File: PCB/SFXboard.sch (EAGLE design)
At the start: 17 parts, among them J1 AVR_SPI_PRG_62X3_LOCK, J2 TERMBLOCK4POS, J3 POWER_JACKPTH, Q1 16MHz, Q2 BSS138, Q3 BSS138, Q4 BSS138, U1 ATMEGA16U2-AU, X1 USBSMD

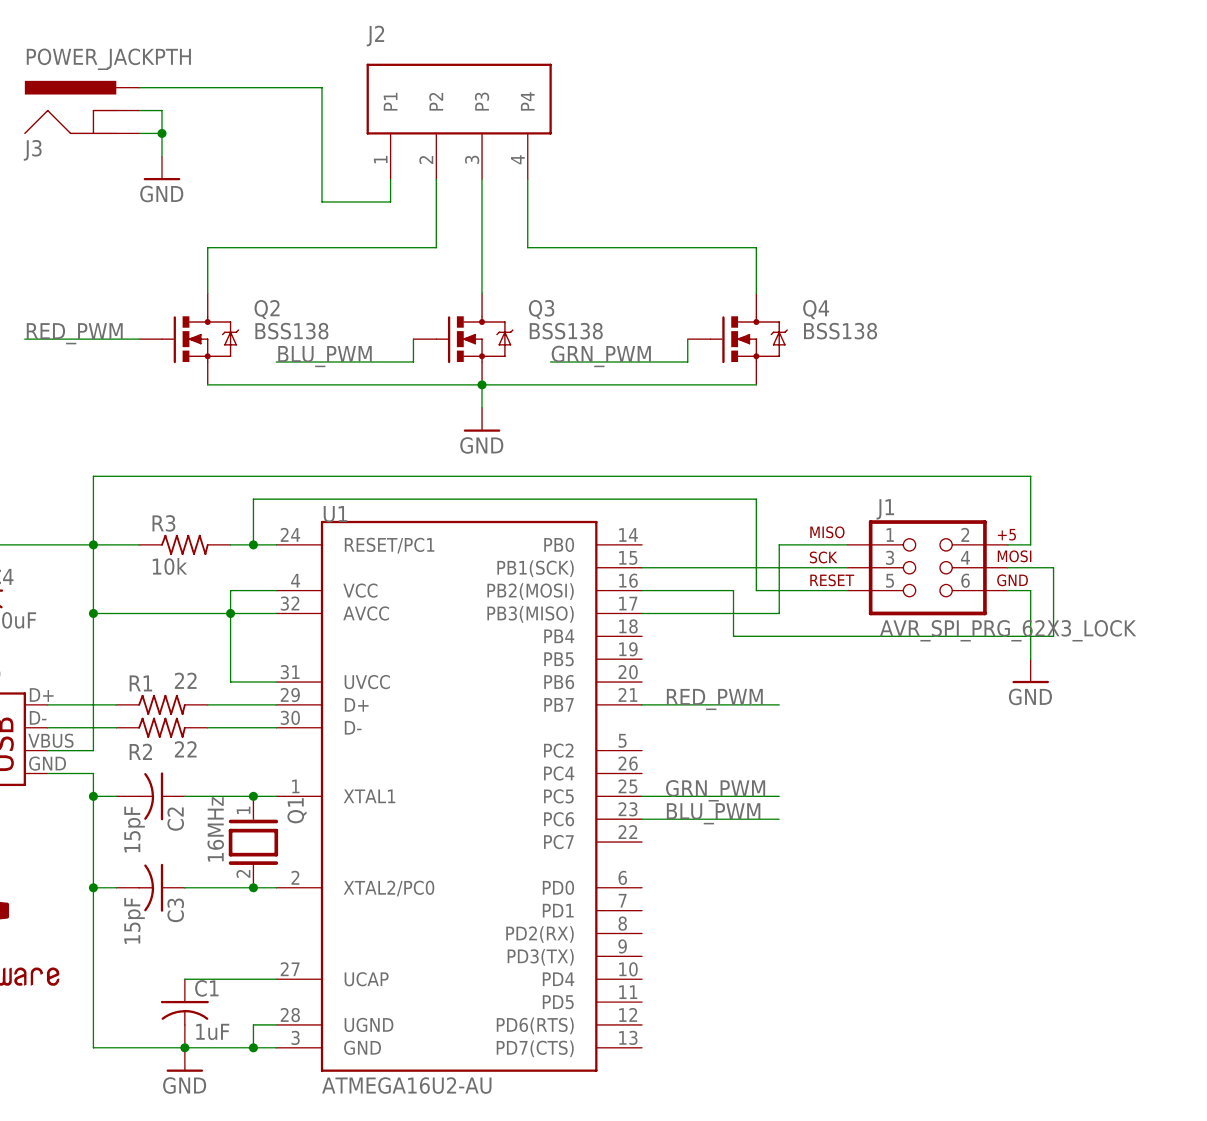
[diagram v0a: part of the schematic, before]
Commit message: Begin working on better power filtering, misc enhancements
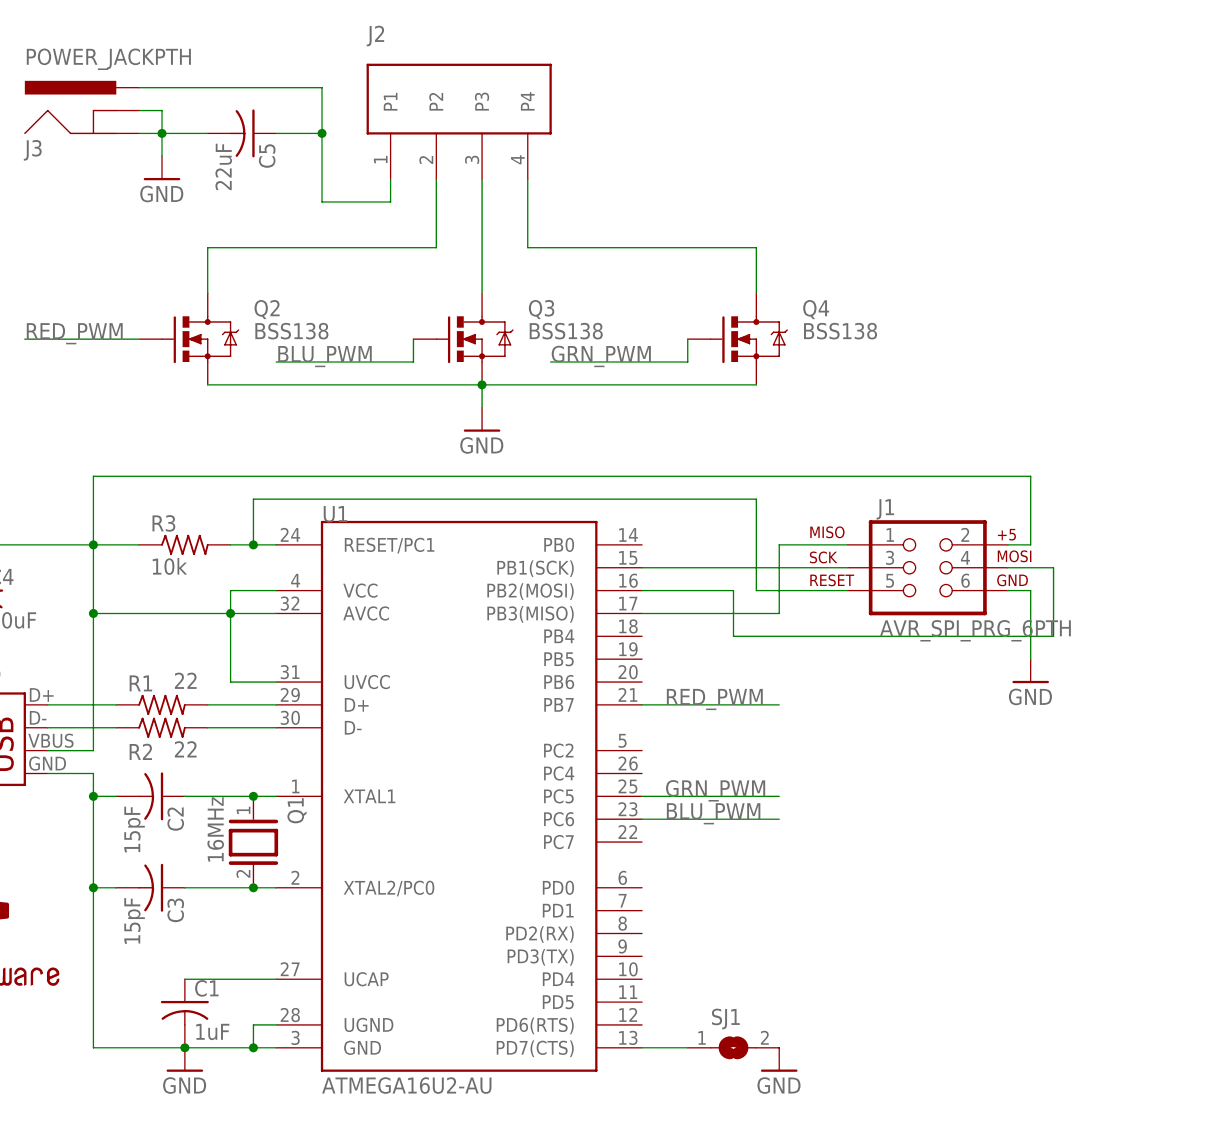
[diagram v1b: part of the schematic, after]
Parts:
- added C5: 22uF, resistor:C-USC0805
- added SJ1: (no value), jumper:SJ
- J1: value AVR_SPI_PRG_62X3_LOCK -> AVR_SPI_PRG_6PTH; device SparkFun-Connectors:AVR_SPI_PRG_62X3_LOCK -> SparkFun-Connectors:AVR_SPI_PRG_6PTH
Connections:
- new net N$17: SJ1.1, U1.PD7(CTS)
- net GND: now also C5.2, SJ1.2
- net N$16: now also C5.1
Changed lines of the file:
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@@
 <part name="C4" library="resistor" deviceset="C-US" device="C0805" value="10uF"/>
 <part name="GND3" library="supply1" deviceset="GND" device=""/>
-<part name="J1" library="SparkFun-Connectors" deviceset="AVR_SPI_PRG_6" device="2X3_LOCK"/>
+<part name="J1" library="SparkFun-Connectors" deviceset="AVR_SPI_PRG_6" device="PTH"/>
 <part name="GND4" library="supply1" deviceset="GND" device=""/>
 <part name="J2" library="sfxboard" deviceset="TERMBLOCK4POS" device=""/>
@@
 <part name="GND5" library="supply1" deviceset="GND" device=""/>
 <part name="U$2" library="SparkFun-Aesthetics" deviceset="OSHW-LOGO" device="S"/>
+<part name="C5" library="resistor" deviceset="C-US" device="C0805" value="22uF"/>
+<part name="SJ1" library="jumper" deviceset="SJ" device=""/>
+<part name="GND6" library="supply1" deviceset="GND" device=""/>
 </parts>
 <sheets>
@@
 <instance part="GND5" gate="1" x="-33.02" y="68.58"/>
 <instance part="U$2" gate="G$1" x="-55.88" y="-12.7"/>
+<instance part="C5" gate="G$1" x="-22.86" y="73.66" rot="R270"/>
+<instance part="SJ1" gate="1" x="30.48" y="-27.94"/>
+<instance part="GND6" gate="1" x="35.56" y="-30.48"/>
 </instances>
 <busses>
@@
 <pinref part="GND5" gate="1" pin="GND"/>
 <junction x="-33.02" y="73.66"/>
+<pinref part="C5" gate="G$1" pin="2"/>
+<wire x1="-27.94" y1="73.66" x2="-33.02" y2="73.66" width="0.1524" layer="91"/>
+</segment>
+<segment>
+<pinref part="SJ1" gate="1" pin="2"/>
+<pinref part="GND6" gate="1" pin="GND"/>
 </segment>
 </net>
@@
 <pinref part="J3" gate="G$1" pin="PWR"/>
 <wire x1="-35.56" y1="78.74" x2="-15.24" y2="78.74" width="0.1524" layer="91"/>
-<wire x1="-15.24" y1="78.74" x2="-15.24" y2="66.04" width="0.1524" layer="91"/>
+<wire x1="-15.24" y1="78.74" x2="-15.24" y2="73.66" width="0.1524" layer="91"/>
+<wire x1="-15.24" y1="73.66" x2="-15.24" y2="66.04" width="0.1524" layer="91"/>
 <wire x1="-15.24" y1="66.04" x2="-7.62" y2="66.04" width="0.1524" layer="91"/>
 <pinref part="J2" gate="G$1" pin="P1"/>
 <wire x1="-7.62" y1="66.04" x2="-7.62" y2="68.58" width="0.1524" layer="91"/>
+<pinref part="C5" gate="G$1" pin="1"/>
+<wire x1="-20.32" y1="73.66" x2="-15.24" y2="73.66" width="0.1524" layer="91"/>
+<junction x="-15.24" y="73.66"/>
 </segment>
 </net>
@@
 </segment>
 </net>
+<net name="N$17" class="0">
+<segment>
+<pinref part="SJ1" gate="1" pin="1"/>
+<pinref part="U1" gate="G$1" pin="PD7(CTS)"/>
+<wire x1="25.4" y1="-27.94" x2="20.32" y2="-27.94" width="0.1524" layer="91"/>
+</segment>
+</net>

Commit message: Circuit improvements, but not yet complete
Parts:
- added C6: 0.1uF, resistor:C-USC0402
- added F1: PTC0603, SparkFun-PowerIC:PTC0603
- added FRAME1: FRAME-LETTER, SparkFun-Aesthetics:FRAME-LETTER
- added R4, R5, R6: 470, resistor:R-US_R0805
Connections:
- new net B: R6.1, U1.PC6
- new net G: R5.1, U1.PC5
- new net N$18: C4.1, C6.1, F1.2, J1.2, R3.1, U1.AVCC, U1.UVCC, U1.VCC
- new net R: R4.1, U1.PB7
- net BLU_PWM: now also R6.2; no longer U1.PC6
- net GND: now also C6.2
- net GRN_PWM: now also R5.2; no longer U1.PC5
- net N$2: now also F1.1; no longer C4.1, J1.2, R3.1, U1.AVCC, U1.UVCC, U1.VCC
- net RED_PWM: now also R4.2; no longer U1.PB7
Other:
- note added: "Karl Koscher (supersat@cs.uw.edu)"
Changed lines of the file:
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@@
 <part name="SJ1" library="jumper" deviceset="SJ" device=""/>
 <part name="GND6" library="supply1" deviceset="GND" device=""/>
+<part name="C6" library="resistor" deviceset="C-US" device="C0402" value="0.1uF"/>
+<part name="GND7" library="supply1" deviceset="GND" device=""/>
+<part name="R4" library="resistor" deviceset="R-US_" device="R0805" value="470"/>
+<part name="R5" library="resistor" deviceset="R-US_" device="R0805" value="470"/>
+<part name="R6" library="resistor" deviceset="R-US_" device="R0805" value="470"/>
+<part name="FRAME1" library="SparkFun-Aesthetics" deviceset="FRAME-LETTER" device=""/>
+<part name="F1" library="SparkFun-PowerIC" deviceset="PTC" device="0603"/>
 </parts>
 <sheets>
 <sheet>
 <plain>
+<text x="26.67" y="-79.248" size="2.54" layer="94">Karl Koscher (supersat@cs.uw.edu)</text>
 </plain>
 <instances>
@@
 <instance part="C1" gate="G$1" x="-30.48" y="-22.86"/>
 <instance part="GND1" gate="1" x="-30.48" y="-30.48"/>
-<instance part="X1" gate="G$1" x="-48.26" y="2.54" rot="MR0"/>
+<instance part="X1" gate="G$1" x="-60.96" y="2.54" rot="MR0"/>
 <instance part="R1" gate="G$1" x="-33.02" y="10.16" smashed="yes">
 <attribute name="NAME" x="-36.83" y="11.6586" size="1.778" layer="95"/>
@@
 <instance part="SJ1" gate="1" x="30.48" y="-27.94"/>
 <instance part="GND6" gate="1" x="35.56" y="-30.48"/>
+<instance part="C6" gate="G$1" x="-63.5" y="22.86"/>
+<instance part="GND7" gate="1" x="-63.5" y="15.24"/>
+<instance part="R4" gate="G$1" x="30.48" y="10.16"/>
+<instance part="R5" gate="G$1" x="30.48" y="0" smashed="yes">
+<attribute name="NAME" x="26.67" y="1.4986" size="1.778" layer="95"/>
+<attribute name="VALUE" x="31.75" y="1.778" size="1.778" layer="96"/>
+</instance>
+<instance part="R6" gate="G$1" x="30.48" y="-2.54" smashed="yes">
+<attribute name="NAME" x="26.67" y="-6.1214" size="1.778" layer="95"/>
+<attribute name="VALUE" x="31.75" y="-5.842" size="1.778" layer="96"/>
+</instance>
+<instance part="FRAME1" gate="G$1" x="-121.92" y="-86.36"/>
+<instance part="FRAME1" gate="G$2" x="25.4" y="-86.36"/>
+<instance part="F1" gate="G$1" x="-50.8" y="5.08"/>
 </instances>
 <busses>
@@
 <wire x1="-40.64" y1="-10.16" x2="-40.64" y2="0" width="0.1524" layer="91"/>
 <wire x1="-40.64" y1="0" x2="-40.64" y2="2.54" width="0.1524" layer="91"/>
-<wire x1="-40.64" y1="2.54" x2="-45.72" y2="2.54" width="0.1524" layer="91"/>
+<wire x1="-40.64" y1="2.54" x2="-58.42" y2="2.54" width="0.1524" layer="91"/>
 <pinref part="C2" gate="G$1" pin="2"/>
 <wire x1="-38.1" y1="0" x2="-40.64" y2="0" width="0.1524" layer="91"/>
@@
 <pinref part="GND6" gate="1" pin="GND"/>
 </segment>
-</net>
-<net name="N$2" class="0">
-<segment>
-<pinref part="U1" gate="G$1" pin="VCC"/>
-<wire x1="-20.32" y1="22.86" x2="-25.4" y2="22.86" width="0.1524" layer="91"/>
-<wire x1="-25.4" y1="22.86" x2="-25.4" y2="20.32" width="0.1524" layer="91"/>
-<pinref part="U1" gate="G$1" pin="AVCC"/>
-<wire x1="-25.4" y1="20.32" x2="-20.32" y2="20.32" width="0.1524" layer="91"/>
-<pinref part="U1" gate="G$1" pin="UVCC"/>
-<wire x1="-20.32" y1="12.7" x2="-25.4" y2="12.7" width="0.1524" layer="91"/>
-<wire x1="-25.4" y1="20.32" x2="-25.4" y2="12.7" width="0.1524" layer="91"/>
-<pinref part="X1" gate="G$1" pin="VBUS"/>
-<wire x1="-45.72" y1="5.08" x2="-40.64" y2="5.08" width="0.1524" layer="91"/>
-<wire x1="-40.64" y1="5.08" x2="-40.64" y2="20.32" width="0.1524" layer="91"/>
-<wire x1="-40.64" y1="20.32" x2="-25.4" y2="20.32" width="0.1524" layer="91"/>
-<junction x="-25.4" y="20.32"/>
-<pinref part="R3" gate="G$1" pin="1"/>
-<wire x1="-35.56" y1="27.94" x2="-40.64" y2="27.94" width="0.1524" layer="91"/>
-<wire x1="-40.64" y1="27.94" x2="-40.64" y2="20.32" width="0.1524" layer="91"/>
-<junction x="-40.64" y="20.32"/>
-<pinref part="C4" gate="G$1" pin="1"/>
-<wire x1="-53.34" y1="25.4" x2="-53.34" y2="27.94" width="0.1524" layer="91"/>
-<wire x1="-53.34" y1="27.94" x2="-40.64" y2="27.94" width="0.1524" layer="91"/>
-<junction x="-40.64" y="27.94"/>
-<pinref part="J1" gate="G$1" pin="2"/>
-<wire x1="60.96" y1="27.94" x2="63.5" y2="27.94" width="0.1524" layer="91"/>
-<wire x1="63.5" y1="27.94" x2="63.5" y2="35.56" width="0.1524" layer="91"/>
-<wire x1="63.5" y1="35.56" x2="-40.64" y2="35.56" width="0.1524" layer="91"/>
-<wire x1="-40.64" y1="35.56" x2="-40.64" y2="27.94" width="0.1524" layer="91"/>
+<segment>
+<pinref part="C6" gate="G$1" pin="2"/>
+<pinref part="GND7" gate="1" pin="GND"/>
 </segment>
 </net>
@@
 <pinref part="X1" gate="G$1" pin="D+"/>
 <pinref part="R1" gate="G$1" pin="1"/>
-<wire x1="-45.72" y1="10.16" x2="-38.1" y2="10.16" width="0.1524" layer="91"/>
+<wire x1="-58.42" y1="10.16" x2="-38.1" y2="10.16" width="0.1524" layer="91"/>
 </segment>
 </net>
@@
 <pinref part="X1" gate="G$1" pin="D-"/>
 <pinref part="R2" gate="G$1" pin="1"/>
-<wire x1="-45.72" y1="7.62" x2="-38.1" y2="7.62" width="0.1524" layer="91"/>
+<wire x1="-58.42" y1="7.62" x2="-38.1" y2="7.62" width="0.1524" layer="91"/>
 </segment>
 </net>
@@
 <net name="RED_PWM" class="0">
 <segment>
-<pinref part="U1" gate="G$1" pin="PB7"/>
-<wire x1="20.32" y1="10.16" x2="35.56" y2="10.16" width="0.1524" layer="91"/>
-<label x="22.86" y="10.16" size="1.778" layer="95"/>
-</segment>
-<segment>
 <pinref part="Q2" gate="G$1" pin="G"/>
 <wire x1="-35.56" y1="50.8" x2="-48.26" y2="50.8" width="0.1524" layer="91"/>
 <label x="-48.26" y="50.8" size="1.778" layer="95"/>
+</segment>
+<segment>
+<pinref part="R4" gate="G$1" pin="2"/>
+<wire x1="35.56" y1="10.16" x2="50.8" y2="10.16" width="0.1524" layer="91"/>
+<label x="38.1" y="10.16" size="1.778" layer="95"/>
 </segment>
 </net>
@@
 </segment>
 <segment>
-<pinref part="U1" gate="G$1" pin="PC6"/>
-<wire x1="20.32" y1="-2.54" x2="35.56" y2="-2.54" width="0.1524" layer="91"/>
-<label x="22.86" y="-2.54" size="1.778" layer="95"/>
+<pinref part="R6" gate="G$1" pin="2"/>
+<wire x1="35.56" y1="-2.54" x2="50.8" y2="-2.54" width="0.1524" layer="91"/>
+<label x="38.1" y="-2.54" size="1.778" layer="95"/>
 </segment>
 </net>
@@
 </segment>
 <segment>
-<pinref part="U1" gate="G$1" pin="PC5"/>
-<wire x1="20.32" y1="0" x2="35.56" y2="0" width="0.1524" layer="91"/>
-<label x="22.86" y="0" size="1.778" layer="95"/>
+<pinref part="R5" gate="G$1" pin="2"/>
+<wire x1="35.56" y1="0" x2="50.8" y2="0" width="0.1524" layer="91"/>
+<label x="38.1" y="0" size="1.778" layer="95"/>
 </segment>
 </net>
@@
 </segment>
 </net>
+<net name="R" class="0">
+<segment>
+<pinref part="U1" gate="G$1" pin="PB7"/>
+<wire x1="20.32" y1="10.16" x2="25.4" y2="10.16" width="0.1524" layer="91"/>
+<pinref part="R4" gate="G$1" pin="1"/>
+</segment>
+</net>
+<net name="G" class="0">
+<segment>
+<pinref part="U1" gate="G$1" pin="PC5"/>
+<wire x1="20.32" y1="0" x2="25.4" y2="0" width="0.1524" layer="91"/>
+<pinref part="R5" gate="G$1" pin="1"/>
+</segment>
+</net>
+<net name="B" class="0">
+<segment>
+<pinref part="U1" gate="G$1" pin="PC6"/>
+<wire x1="20.32" y1="-2.54" x2="25.4" y2="-2.54" width="0.1524" layer="91"/>
+<pinref part="R6" gate="G$1" pin="1"/>
+</segment>
+</net>
+<net name="N$18" class="0">
+<segment>
+<pinref part="U1" gate="G$1" pin="VCC"/>
+<wire x1="-20.32" y1="22.86" x2="-25.4" y2="22.86" width="0.1524" layer="91"/>
+<wire x1="-25.4" y1="22.86" x2="-25.4" y2="20.32" width="0.1524" layer="91"/>
+<pinref part="U1" gate="G$1" pin="AVCC"/>
+<wire x1="-25.4" y1="20.32" x2="-20.32" y2="20.32" width="0.1524" layer="91"/>
+<pinref part="U1" gate="G$1" pin="UVCC"/>
+<wire x1="-20.32" y1="12.7" x2="-25.4" y2="12.7" width="0.1524" layer="91"/>
+<wire x1="-25.4" y1="20.32" x2="-25.4" y2="12.7" width="0.1524" layer="91"/>
+<wire x1="-40.64" y1="20.32" x2="-25.4" y2="20.32" width="0.1524" layer="91"/>
+<junction x="-25.4" y="20.32"/>
+<pinref part="R3" gate="G$1" pin="1"/>
+<wire x1="-35.56" y1="27.94" x2="-40.64" y2="27.94" width="0.1524" layer="91"/>
+<wire x1="-40.64" y1="27.94" x2="-40.64" y2="20.32" width="0.1524" layer="91"/>
+<pinref part="C4" gate="G$1" pin="1"/>
+<wire x1="-53.34" y1="25.4" x2="-53.34" y2="27.94" width="0.1524" layer="91"/>
+<wire x1="-53.34" y1="27.94" x2="-40.64" y2="27.94" width="0.1524" layer="91"/>
+<junction x="-40.64" y="27.94"/>
+<pinref part="J1" gate="G$1" pin="2"/>
+<wire x1="60.96" y1="27.94" x2="63.5" y2="27.94" width="0.1524" layer="91"/>
+<wire x1="63.5" y1="27.94" x2="63.5" y2="35.56" width="0.1524" layer="91"/>
+<wire x1="63.5" y1="35.56" x2="-40.64" y2="35.56" width="0.1524" layer="91"/>
+<wire x1="-40.64" y1="35.56" x2="-40.64" y2="27.94" width="0.1524" layer="91"/>
+<pinref part="C6" gate="G$1" pin="1"/>
+<wire x1="-53.34" y1="27.94" x2="-63.5" y2="27.94" width="0.1524" layer="91"/>
+<wire x1="-63.5" y1="27.94" x2="-63.5" y2="25.4" width="0.1524" layer="91"/>
+<junction x="-53.34" y="27.94"/>
+<wire x1="-40.64" y1="5.08" x2="-40.64" y2="20.32" width="0.1524" layer="91"/>
+<junction x="-40.64" y="20.32"/>
+<pinref part="F1" gate="G$1" pin="2"/>
+<wire x1="-40.64" y1="5.08" x2="-43.18" y2="5.08" width="0.1524" layer="91"/>
+</segment>
+</net>
+<net name="N$2" class="0">
+<segment>
+<pinref part="F1" gate="G$1" pin="1"/>
+<pinref part="X1" gate="G$1" pin="VBUS"/>
+<wire x1="-55.88" y1="5.08" x2="-58.42" y2="5.08" width="0.1524" layer="91"/>
+</segment>
+</net>
